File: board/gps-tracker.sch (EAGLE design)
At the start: 30 parts, among them J2 AVR_SPI_PRG_6OFFSET_PADS, U2 MCP73831, U3 ATMEGA328P, X1 USBSMD

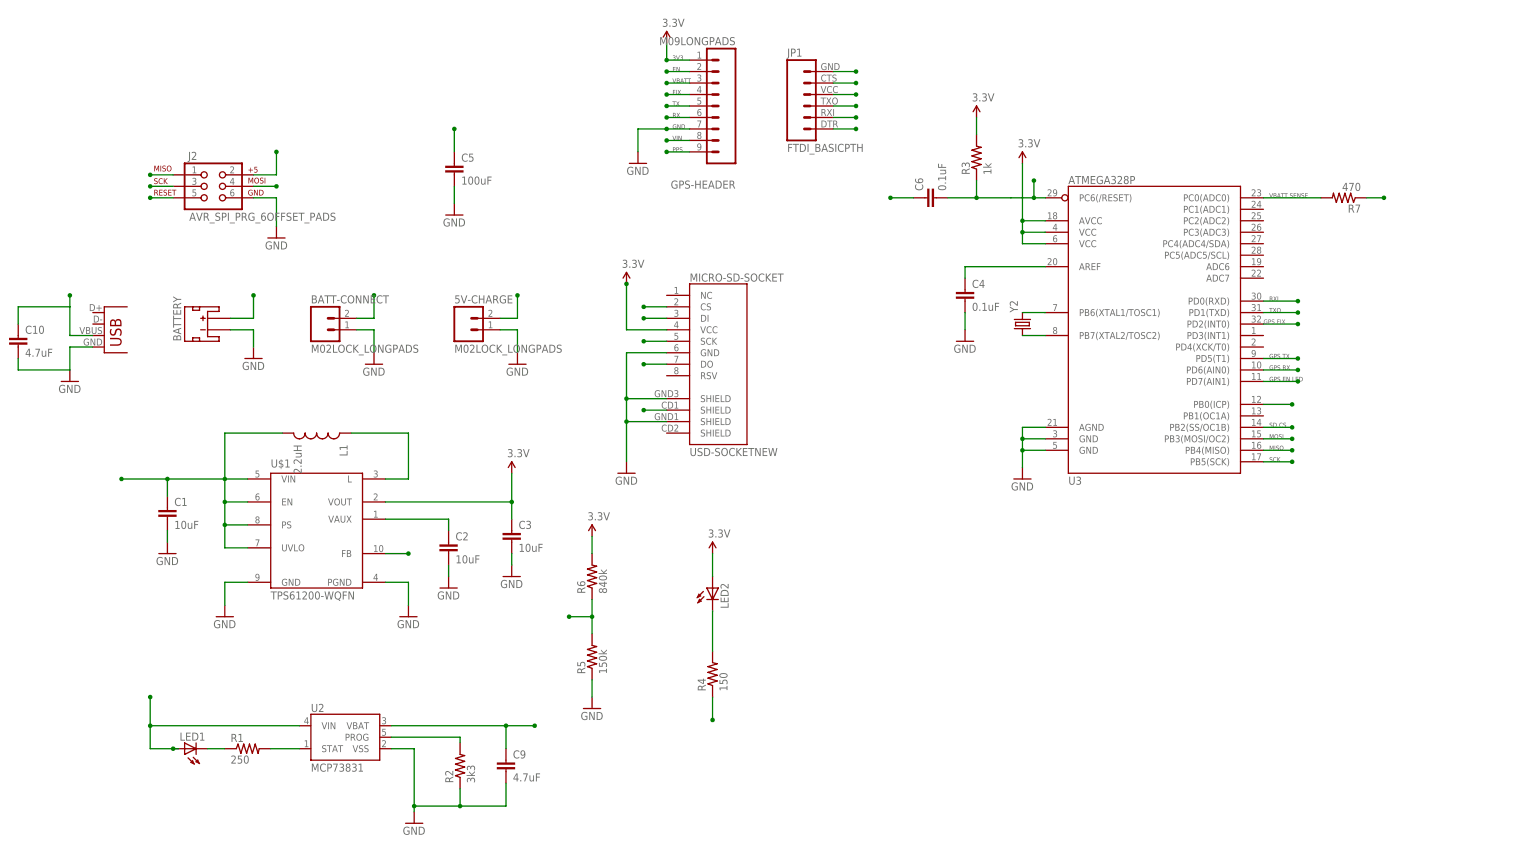
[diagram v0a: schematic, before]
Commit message: Updating board to correct for previous errors, adding another status LED and bringing out the GPS EN pin to the arduino
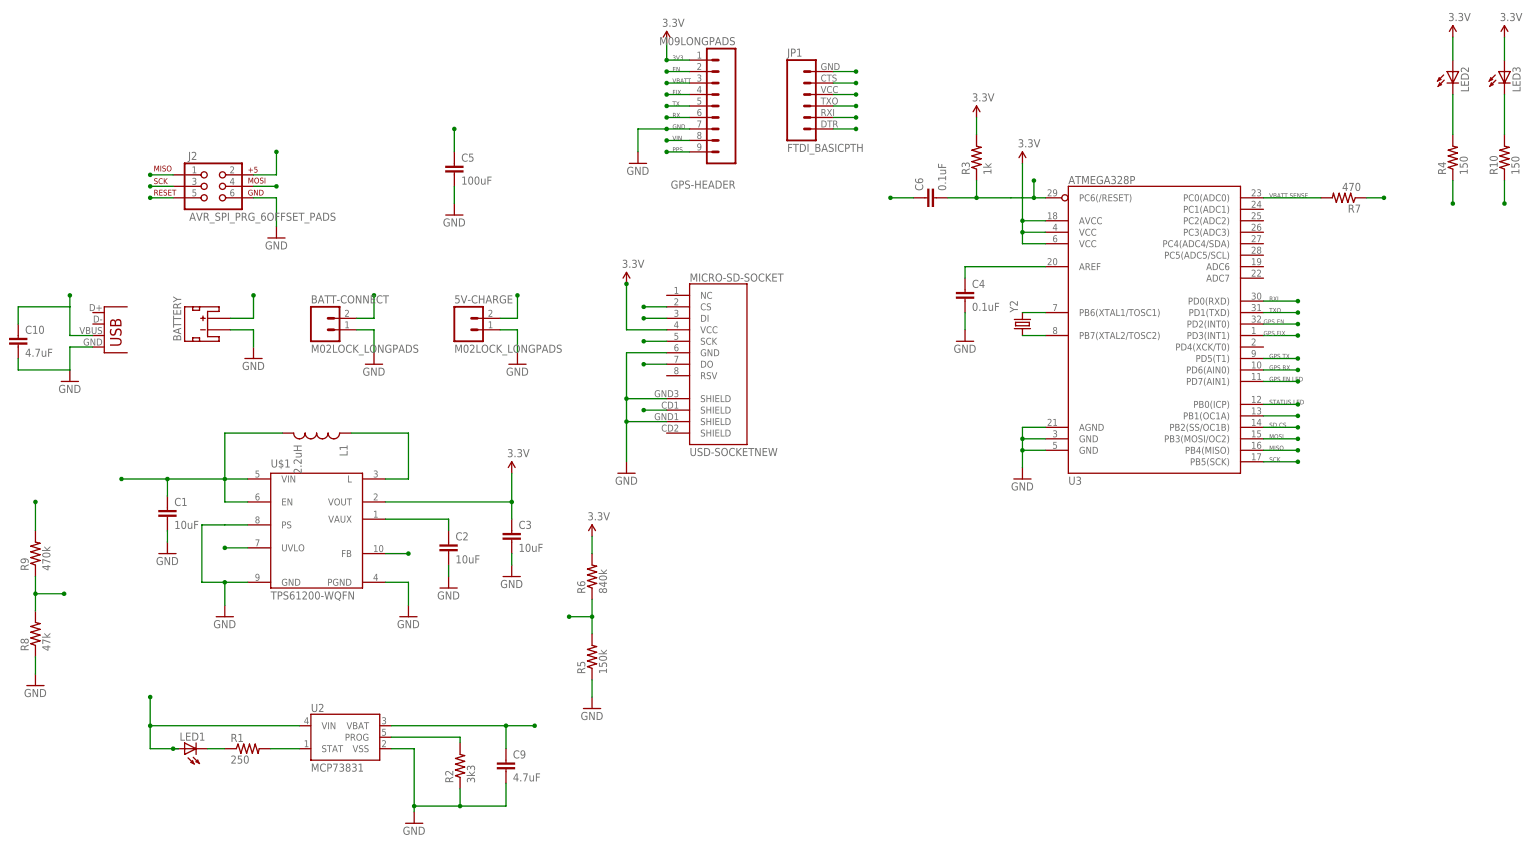
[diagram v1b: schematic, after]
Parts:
- added LED3: (no value), SparkFun-LED:LED0603
- added R10: 150, SparkFun:RESISTOR0805-RES
- added R8: 47k, SparkFun:RESISTOR0603-RES
- added R9: 470k, SparkFun:RESISTOR0603-RES
- LED2: device SparkFun-LED:LED5MM -> SparkFun-LED:LED0603
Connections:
- net BATT_LED renamed STATUS_LED
- removed net EN: GPS-HEADER.2
- new net ALT_STATUS_LED: R10.1, U3.PB1(OC1A)
- new net GPS_EN: GPS-HEADER.2, U3.PD2(INT0)
- new net N$18: LED3.C, R10.2
- new net UVLO: R8.2, R9.1, U$1.UVLO
- net 3.3V: now also LED3.A
- net GND: now also R8.1, U$1.PS
- net GPS_FIX: now also U3.PD3(INT1); no longer U3.PD2(INT0)
- net RXI: now also JP1.2; no longer JP1.3
- net TXO: now also JP1.3; no longer JP1.2
- net VBATT: now also R9.2; no longer U$1.PS, U$1.UVLO
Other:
- note added: "GPS EN"
- note added: "STATUS LED"
- moved on the sheet: LED2, R4
